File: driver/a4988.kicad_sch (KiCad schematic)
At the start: 5 parts

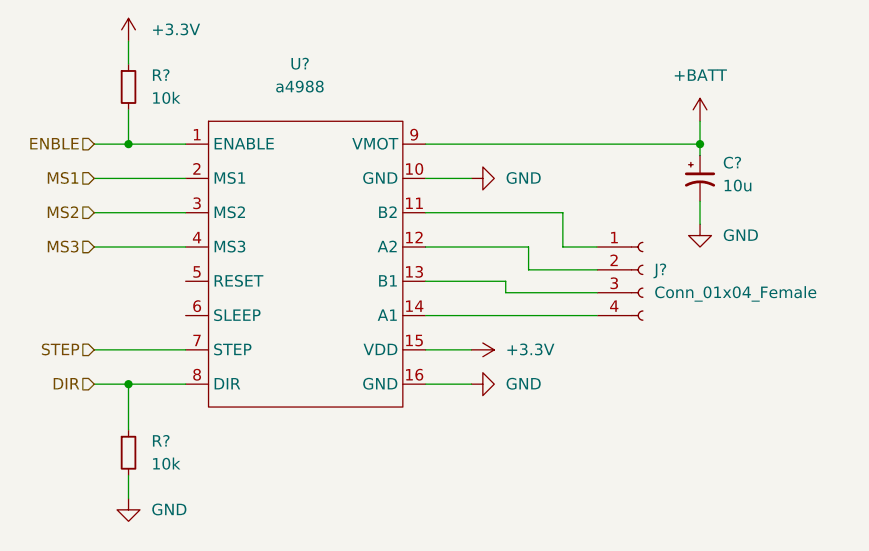
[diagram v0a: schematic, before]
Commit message: 部品配置完了
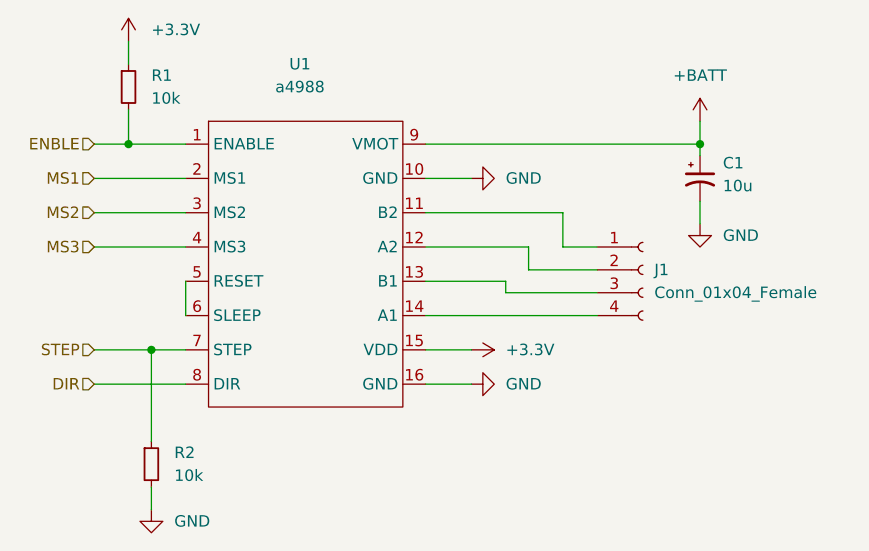
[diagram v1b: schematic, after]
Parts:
- C1: renamed from C?; footprint (none) -> Capacitor_THT:CP_Radial_D5.0mm_P2.50mm
- J1: renamed from J?; footprint (none) -> Connector_PinSocket_2.54mm:PinSocket_1x04_P2.54mm_Horizontal
- R1, R2: renamed from R?; footprint (none) -> Resistor_SMD:R_0805_2012Metric_Pad1.20x1.40mm_HandSolder
- U1: renamed from U?; footprint (none) -> stepper_music_lib:a4988
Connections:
- net DIR: no longer R2.1
- net STEP: now also R2.1
- net at U1.5 (RESET): now also U1.6 (SLEEP)
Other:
- moved on the sheet: R2
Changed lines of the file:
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@@
 (kicad_sch (version 20211123) (generator eeschema)
   (paper "A4")
-  (junction (at 123.19 96.52) (diameter 0) (color 0 0 0 0)
-  )
   (junction (at 123.19 69.85) (diameter 0) (color 0 0 0 0)
   )
   (junction (at 186.69 69.85) (diameter 0) (color 0 0 0 0)
   )
+  (junction (at 125.73 92.71) (diameter 0) (color 0 0 0 0)
+  )
   (wire (pts (xy 156.21 73.66) (xy 161.29 73.66))
     (stroke (width 0) (type default) (color 0 0 0 0))
@@
     (stroke (width 0) (type default) (color 0 0 0 0))
   )
+  (wire (pts (xy 129.54 85.09) (xy 129.54 88.9))
+    (stroke (width 0) (type default) (color 0 0 0 0))
+  )
   (wire (pts (xy 167.64 81.28) (xy 167.64 83.82))
     (stroke (width 0) (type default) (color 0 0 0 0))
@@
     (stroke (width 0) (type default) (color 0 0 0 0))
   )
+  (wire (pts (xy 125.73 92.71) (xy 125.73 102.87))
+    (stroke (width 0) (type default) (color 0 0 0 0))
+  )
   (wire (pts (xy 156.21 88.9) (xy 175.26 88.9))
     (stroke (width 0) (type default) (color 0 0 0 0))
@@
     (stroke (width 0) (type default) (color 0 0 0 0))
   )
-  (wire (pts (xy 123.19 101.6) (xy 123.19 96.52))
-    (stroke (width 0) (type default) (color 0 0 0 0))
-  )
   (wire (pts (xy 156.21 92.71) (xy 161.29 92.71))
     (stroke (width 0) (type default) (color 0 0 0 0))
@@
     (stroke (width 0) (type default) (color 0 0 0 0))
   )
+  (wire (pts (xy 125.73 92.71) (xy 129.54 92.71))
+    (stroke (width 0) (type default) (color 0 0 0 0))
+  )
   (wire (pts (xy 119.38 73.66) (xy 129.54 73.66))
     (stroke (width 0) (type default) (color 0 0 0 0))
@@
     (stroke (width 0) (type default) (color 0 0 0 0))
   )
-  (wire (pts (xy 119.38 92.71) (xy 129.54 92.71))
+  (wire (pts (xy 119.38 92.71) (xy 125.73 92.71))
     (stroke (width 0) (type default) (color 0 0 0 0))
   )
@@
     (stroke (width 0) (type default) (color 0 0 0 0))
   )
-  (wire (pts (xy 119.38 96.52) (xy 123.19 96.52))
-    (stroke (width 0) (type default) (color 0 0 0 0))
-  )
-  (wire (pts (xy 123.19 96.52) (xy 129.54 96.52))
-    (stroke (width 0) (type default) (color 0 0 0 0))
-  )
-  (wire (pts (xy 123.19 106.68) (xy 123.19 109.22))
+  (wire (pts (xy 119.38 96.52) (xy 129.54 96.52))
+    (stroke (width 0) (type default) (color 0 0 0 0))
+  )
+  (wire (pts (xy 125.73 107.95) (xy 125.73 110.49))
     (stroke (width 0) (type default) (color 0 0 0 0))
   )
@@
   (symbol (lib_id "Connector:Conn_01x04_Female") (at 180.34 83.82 0) (unit 1)
     (in_bom yes) (on_board yes) (fields_autoplaced)
-    (property "Reference" "J?" (id 0) (at 181.61 83.8199 0)
+    (property "Reference" "J1" (id 0) (at 181.61 83.8199 0)
       (effects (font (size 1.27 1.27)) (justify left))
     )
@@
       (effects (font (size 1.27 1.27)) (justify left))
     )
-    (property "Footprint" "" (id 2) (at 180.34 83.82 0)
+    (property "Footprint" "Connector_PinSocket_2.54mm:PinSocket_1x04_P2.54mm_Horizontal" (id 2) (at 180.34 83.82 0)
       (effects (font (size 1.27 1.27)) hide)
     )
@@
   (symbol (lib_id "power:GND") (at 161.29 73.66 90) (unit 1)
     (in_bom yes) (on_board yes) (fields_autoplaced)
-    (property "Reference" "#PWR?" (id 0) (at 167.64 73.66 0)
+    (property "Reference" "#PWR03" (id 0) (at 167.64 73.66 0)
       (effects (font (size 1.27 1.27)) hide)
     )
@@
   (symbol (lib_id "Device:R_Small") (at 123.19 63.5 0) (unit 1)
     (in_bom yes) (on_board yes) (fields_autoplaced)
-    (property "Reference" "R?" (id 0) (at 125.73 62.2299 0)
+    (property "Reference" "R1" (id 0) (at 125.73 62.2299 0)
       (effects (font (size 1.27 1.27)) (justify left))
     )
@@
       (effects (font (size 1.27 1.27)) (justify left))
     )
-    (property "Footprint" "" (id 2) (at 123.19 63.5 0)
+    (property "Footprint" "Resistor_SMD:R_0805_2012Metric_Pad1.20x1.40mm_HandSolder" (id 2) (at 123.19 63.5 0)
       (effects (font (size 1.27 1.27)) hide)
     )
@@
   (symbol (lib_id "power:GND") (at 186.69 78.74 0) (unit 1)
     (in_bom yes) (on_board yes) (fields_autoplaced)
-    (property "Reference" "#PWR?" (id 0) (at 186.69 85.09 0)
+    (property "Reference" "#PWR07" (id 0) (at 186.69 85.09 0)
       (effects (font (size 1.27 1.27)) hide)
     )
@@
   (symbol (lib_id "Device:C_Polarized_Small_US") (at 186.69 73.66 0) (unit 1)
     (in_bom yes) (on_board yes) (fields_autoplaced)
-    (property "Reference" "C?" (id 0) (at 189.23 71.9581 0)
+    (property "Reference" "C1" (id 0) (at 189.23 71.9581 0)
       (effects (font (size 1.27 1.27)) (justify left))
     )
@@
       (effects (font (size 1.27 1.27)) (justify left))
     )
-    (property "Footprint" "" (id 2) (at 186.69 73.66 0)
+    (property "Footprint" "Capacitor_THT:CP_Radial_D5.0mm_P2.50mm" (id 2) (at 186.69 73.66 0)
       (effects (font (size 1.27 1.27)) hide)
     )
@@
   (symbol (lib_id "stepper_music_lib:a4988") (at 143.51 62.23 0) (unit 1)
     (in_bom yes) (on_board yes)
-    (property "Reference" "U?" (id 0) (at 142.24 60.96 0))
+    (property "Reference" "U1" (id 0) (at 142.24 60.96 0))
     (property "Value" "a4988" (id 1) (at 142.24 63.5 0))
-    (property "Footprint" "" (id 2) (at 143.51 62.23 0)
+    (property "Footprint" "stepper_music_lib:a4988" (id 2) (at 143.51 62.23 0)
       (effects (font (size 1.27 1.27)) hide)
     )
@@
   (symbol (lib_id "power:+BATT") (at 186.69 67.31 0) (unit 1)
     (in_bom yes) (on_board yes) (fields_autoplaced)
-    (property "Reference" "#PWR?" (id 0) (at 186.69 71.12 0)
+    (property "Reference" "#PWR06" (id 0) (at 186.69 71.12 0)
       (effects (font (size 1.27 1.27)) hide)
     )
@@
   (symbol (lib_id "power:+3.3V") (at 123.19 58.42 0) (unit 1)
     (in_bom yes) (on_board yes) (fields_autoplaced)
-    (property "Reference" "#PWR?" (id 0) (at 123.19 62.23 0)
+    (property "Reference" "#PWR01" (id 0) (at 123.19 62.23 0)
       (effects (font (size 1.27 1.27)) hide)
     )
@@
   (symbol (lib_id "power:+3.3V") (at 161.29 92.71 270) (unit 1)
     (in_bom yes) (on_board yes) (fields_autoplaced)
-    (property "Reference" "#PWR?" (id 0) (at 157.48 92.71 0)
+    (property "Reference" "#PWR04" (id 0) (at 157.48 92.71 0)
       (effects (font (size 1.27 1.27)) hide)
     )
@@
   (symbol (lib_id "power:GND") (at 161.29 96.52 90) (unit 1)
     (in_bom yes) (on_board yes) (fields_autoplaced)
-    (property "Reference" "#PWR?" (id 0) (at 167.64 96.52 0)
+    (property "Reference" "#PWR05" (id 0) (at 167.64 96.52 0)
       (effects (font (size 1.27 1.27)) hide)
     )
@@
     (pin "1")
   )
-  (symbol (lib_id "power:GND") (at 123.19 109.22 0) (unit 1)
-    (in_bom yes) (on_board yes) (fields_autoplaced)
-    (property "Reference" "#PWR?" (id 0) (at 123.19 115.57 0)
-      (effects (font (size 1.27 1.27)) hide)
-    )
-    (property "Value" "GND" (id 1) (at 125.73 110.4899 0)
-      (effects (font (size 1.27 1.27)) (justify left))
-    )
-    (property "Footprint" "" (id 2) (at 123.19 109.22 0)
-      (effects (font (size 1.27 1.27)) hide)
-    )
-    (property "Datasheet" "" (id 3) (at 123.19 109.22 0)
-      (effects (font (size 1.27 1.27)) hide)
-    )
-    (pin "1")
-  )
-  (symbol (lib_id "Device:R_Small") (at 123.19 104.14 0) (unit 1)
-    (in_bom yes) (on_board yes) (fields_autoplaced)
-    (property "Reference" "R?" (id 0) (at 125.73 102.8699 0)
-      (effects (font (size 1.27 1.27)) (justify left))
-    )
-    (property "Value" "10k" (id 1) (at 125.73 105.4099 0)
-      (effects (font (size 1.27 1.27)) (justify left))
-    )
-    (property "Footprint" "" (id 2) (at 123.19 104.14 0)
-      (effects (font (size 1.27 1.27)) hide)
-    )
-    (property "Datasheet" "~" (id 3) (at 123.19 104.14 0)
-      (effects (font (size 1.27 1.27)) hide)
-    )
+  (symbol (lib_id "power:GND") (at 125.73 110.49 0) (unit 1)
+    (in_bom yes) (on_board yes) (fields_autoplaced)
+    (property "Reference" "#PWR02" (id 0) (at 125.73 116.84 0)
+      (effects (font (size 1.27 1.27)) hide)
+    )
+    (property "Value" "GND" (id 1) (at 128.27 111.7599 0)
+      (effects (font (size 1.27 1.27)) (justify left))
+    )
+    (property "Footprint" "" (id 2) (at 125.73 110.49 0)
+      (effects (font (size 1.27 1.27)) hide)
+    )
+    (property "Datasheet" "" (id 3) (at 125.73 110.49 0)
+      (effects (font (size 1.27 1.27)) hide)
+    )
+    (pin "1")
+  )
+  (symbol (lib_id "Device:R_Small") (at 125.73 105.41 0) (unit 1)
+    (in_bom yes) (on_board yes) (fields_autoplaced)
+    (property "Reference" "R2" (id 0) (at 128.27 104.1399 0)
+      (effects (font (size 1.27 1.27)) (justify left))
+    )
+    (property "Value" "10k" (id 1) (at 128.27 106.6799 0)
+      (effects (font (size 1.27 1.27)) (justify left))
+    )
+    (property "Footprint" "Resistor_SMD:R_0805_2012Metric_Pad1.20x1.40mm_HandSolder" (id 2) (at 125.73 105.41 0)
+      (effects (font (size 1.27 1.27)) hide)
+    )
+    (property "Datasheet" "~" (id 3) (at 125.73 105.41 0)
+      (effects (font (size 1.27 1.27)) hide)
+    )
